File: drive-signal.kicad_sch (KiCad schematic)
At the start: 25 parts, among them J1 Conn_01x03_Pin, J10 Conn_01x04_Pin, J11 Conn_01x04_Pin, J2 Conn_01x03_Pin, J3 Conn_01x03_Pin, J4 Conn_01x03_Pin, J5 Conn_01x03_Pin, J6 Conn_01x03_Pin, J7 Conn_01x02_Pin, J8 Conn_01x04_Pin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

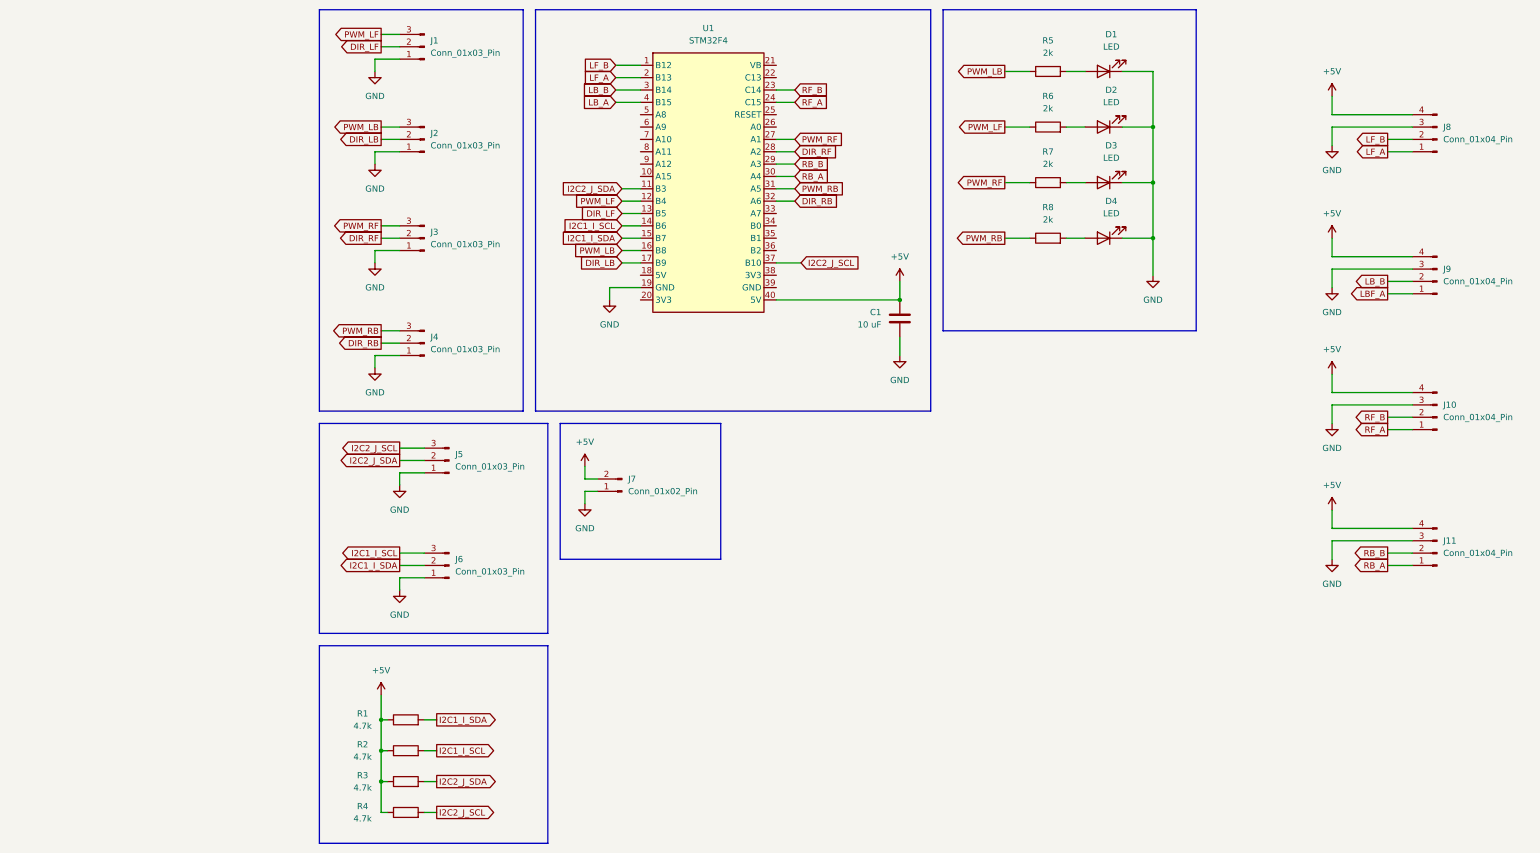
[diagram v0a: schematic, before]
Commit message: fix MD30 pinout
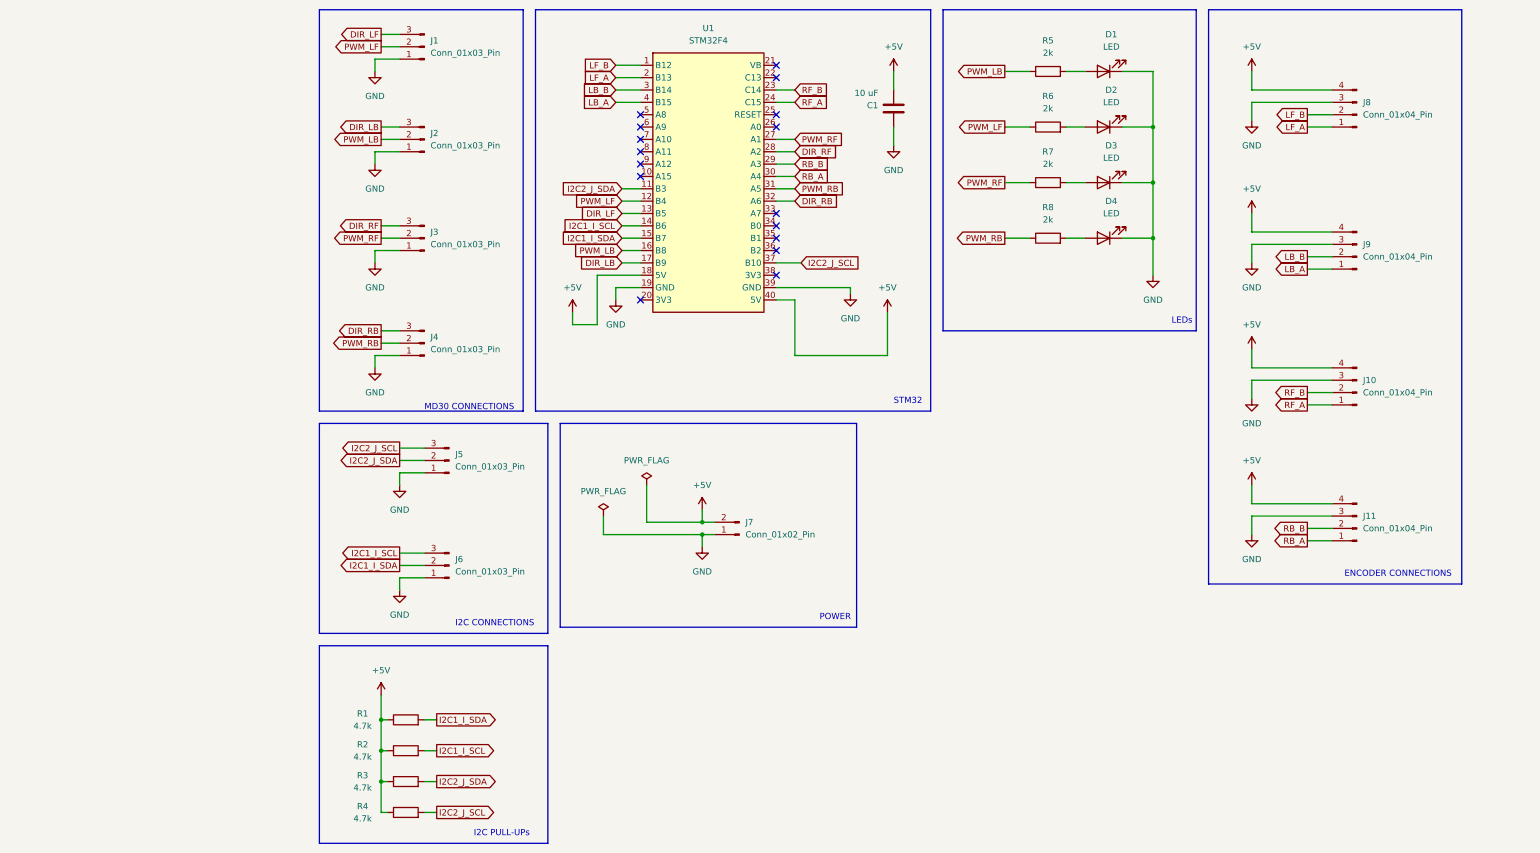
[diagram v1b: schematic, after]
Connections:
- net LBF_A is gone; now on net LB_A: J9.1 (Pin_1)
- net +5V: now also U1.18 (5V)
- net DIR_LB: now also J2.3 (Pin_3); no longer J2.2 (Pin_2)
- net DIR_LF: now also J1.3 (Pin_3); no longer J1.2 (Pin_2)
- net DIR_RB: now also J4.3 (Pin_3); no longer J4.2 (Pin_2)
- net DIR_RF: now also J3.3 (Pin_3); no longer J3.2 (Pin_2)
- net GND: now also U1.39 (GND)
- net PWM_LB: now also J2.2 (Pin_2); no longer J2.3 (Pin_3)
- net PWM_LF: now also J1.2 (Pin_2); no longer J1.3 (Pin_3)
- net PWM_RB: now also J4.2 (Pin_2); no longer J4.3 (Pin_3)
- net PWM_RF: now also J3.2 (Pin_2); no longer J3.3 (Pin_3)
- no-connect marks 0 -> 16
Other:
- note added: "ENCODER CONNECTIONS"
- note added: "I2C CONNECTIONS"
- note added: "I2C PULL-UPs"
- note added: "LEDs"
- note added: "MD30 CONNECTIONS"
- note added: "POWER"
- note added: "STM32"
- company: (none) -> Team RoverX
- title: (none) -> Drive Signal
- moved on the sheet: C1, J10, J11, J7, J8, J9

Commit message: incorporate feedback
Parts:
- J6: value Conn_01x03_Pin -> Conn_01x04_Pin; footprint Connector_JST:JST_PH_B3B-PH-K_1x03_P2.00mm_Vertical -> Connector_JST:JST_PH_B4B-PH-K_1x04_P2.00mm_Vertical; symbol Connector:Conn_01x03_Pin -> Connector:Conn_01x04_Pin
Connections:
- net +5V: now also J6.2 (Pin_2)
- net I2C1_I_SCL: now also J6.4 (Pin_4); no longer J6.3 (Pin_3)
- net I2C1_I_SDA: now also J6.3 (Pin_3); no longer J6.2 (Pin_2)
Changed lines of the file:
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@@
+    (stroke (width 0) (type default))
+  )
+  (wire (pts (xy 17.78 128.27) (xy 35.56 128.27))
     (stroke (width 0) (type default))
   )
@@
     (stroke (width 0) (type default))
   )
+  (wire (pts (xy 17.78 120.65) (xy 17.78 128.27))
+    (stroke (width 0) (type default))
+  )
   (wire (pts (xy 30.48 43.18) (xy 25.4 43.18))
     (stroke (width 0) (type default))
@@
     (stroke (width 0) (type default))
   )
-  (wire (pts (xy 30.48 128.27) (xy 35.56 128.27))
-    (stroke (width 0) (type default))
-  )
   (wire (pts (xy 26.67 160.02) (xy 26.67 166.37))
     (stroke (width 0) (type default))
@@
     (stroke (width 0) (type default))
   )
+  (wire (pts (xy 33.02 123.19) (xy 35.56 123.19))
+    (stroke (width 0) (type default))
+  )
   (wire (pts (xy 74.93 33.02) (xy 80.01 33.02))
     (stroke (width 0) (type default))
   )
+  (wire (pts (xy 33.02 125.73) (xy 35.56 125.73))
+    (stroke (width 0) (type default))
+  )
   (wire (pts (xy 30.48 106.68) (xy 35.56 106.68))
     (stroke (width 0) (type default))
@@
   )
   (wire (pts (xy 26.67 60.96) (xy 30.48 60.96))
-    (stroke (width 0) (type default))
-  )
-  (wire (pts (xy 30.48 125.73) (xy 35.56 125.73))
     (stroke (width 0) (type default))
   )
@@
     )
   )
-  (global_label "I2C1_I_SDA" (shape output) (at 30.48 128.27 180) (fields_autoplaced)
-    (effects (font (size 1.27 1.27)) (justify right))
-    (property "Intersheetrefs" "${INTERSHEET_REFS}" (at 17.0929 128.27 0)
+  (global_label "I2C1_I_SDA" (shape output) (at 33.02 125.73 180) (fields_autoplaced)
+    (effects (font (size 1.27 1.27)) (justify right))
+    (property "Intersheetrefs" "${INTERSHEET_REFS}" (at 19.6329 125.73 0)
       (effects (font (size 1.27 1.27)) (justify right) hide)
     )
@@
     )
   )
-  (global_label "I2C1_I_SCL" (shape output) (at 30.48 125.73 180) (fields_autoplaced)
-    (effects (font (size 1.27 1.27)) (justify right))
-    (property "Intersheetrefs" "${INTERSHEET_REFS}" (at 17.1534 125.73 0)
+  (global_label "I2C1_I_SCL" (shape output) (at 33.02 123.19 180) (fields_autoplaced)
+    (effects (font (size 1.27 1.27)) (justify right))
+    (property "Intersheetrefs" "${INTERSHEET_REFS}" (at 19.6934 123.19 0)
       (effects (font (size 1.27 1.27)) (justify right) hide)
     )
@@
     )
   )
-  (symbol (lib_id "Connector:Conn_01x03_Pin") (at 40.64 128.27 180) (unit 1)
-    (in_bom yes) (on_board yes) (dnp no) (fields_autoplaced)
-    (property "Reference" "J6" (at 41.91 127 0)
-      (effects (font (size 1.27 1.27)) (justify right))
-    )
-    (property "Value" "Conn_01x03_Pin" (at 41.91 129.54 0)
-      (effects (font (size 1.27 1.27)) (justify right))
-    )
-    (property "Footprint" "Connector_JST:JST_PH_B3B-PH-K_1x03_P2.00mm_Vertical" (at 40.64 128.27 0)
+  (symbol (lib_id "Connector:Conn_01x04_Pin") (at 40.64 128.27 180) (unit 1)
+    (in_bom yes) (on_board yes) (dnp no) (fields_autoplaced)
+    (property "Reference" "J6" (at 41.91 125.73 0)
+      (effects (font (size 1.27 1.27)) (justify right))
+    )
+    (property "Value" "Conn_01x04_Pin" (at 41.91 128.27 0)
+      (effects (font (size 1.27 1.27)) (justify right))
+    )
+    (property "Footprint" "Connector_JST:JST_PH_B4B-PH-K_1x04_P2.00mm_Vertical" (at 40.64 128.27 0)
       (effects (font (size 1.27 1.27)) hide)
     )
@@
     (pin "1")
     (pin "3")
+    (pin "4")
     (instances
       (project "drive-signal"
@@
         )
       )
+    )
+  )
+  (symbol (lib_id "power:+5V") (at 17.78 120.65 0) (unit 1)
+    (in_bom yes) (on_board yes) (dnp no) (fields_autoplaced)
+    (property "Reference" "#PWR025" (at 17.78 124.46 0)
+      (effects (font (size 1.27 1.27)) hide)
+    )
+    (property "Value" "+5V" (at 17.78 115.57 0)
+      (effects (font (size 1.27 1.27)))
+    )
+    (property "Footprint" "" (at 17.78 120.65 0)
+      (effects (font (size 1.27 1.27)) hide)
+    )
+    (property "Datasheet" "" (at 17.78 120.65 0)
+      (effects (font (size 1.27 1.27)) hide)
+    )
+    (pin "1")
+    (instances
+      (project "drive-signal"
+        (path "/0fd5a227-32c1-4fb8-b9b0-22b52f16b2f2"
+          (reference "#PWR025") (unit 1)
+        )
+      )

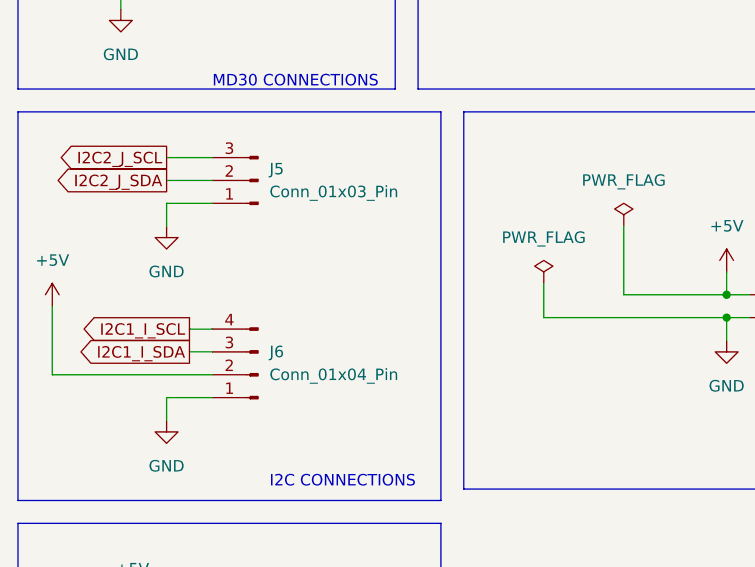
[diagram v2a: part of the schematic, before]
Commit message: make JSTs horizontal
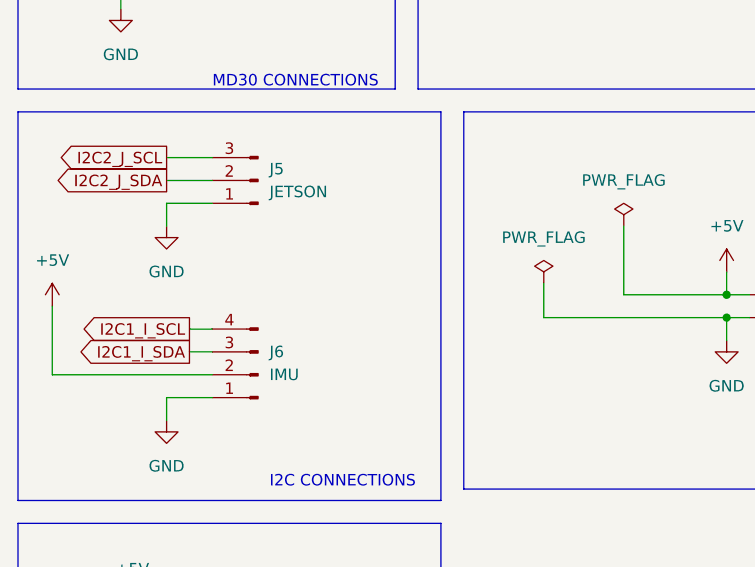
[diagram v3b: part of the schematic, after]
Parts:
- J1, J2, J3, J4: footprint Connector_JST:JST_PH_B3B-PH-K_1x03_P2.00mm_Vertical -> Connector_JST:JST_PH_S3B-PH-K_1x03_P2.00mm_Horizontal
- J10, J11, J8, J9: footprint Connector_JST:JST_PH_B4B-PH-K_1x04_P2.00mm_Vertical -> Connector_JST:JST_PH_S4B-PH-K_1x04_P2.00mm_Horizontal
- J5: value Conn_01x03_Pin -> JETSON
- J6: value Conn_01x04_Pin -> IMU
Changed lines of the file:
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@@
       (effects (font (size 1.27 1.27)) (justify right))
     )
-    (property "Footprint" "Connector_JST:JST_PH_B4B-PH-K_1x04_P2.00mm_Vertical" (at 227.33 35.56 0)
+    (property "Footprint" "Connector_JST:JST_PH_S4B-PH-K_1x04_P2.00mm_Horizontal" (at 227.33 35.56 0)
       (effects (font (size 1.27 1.27)) hide)
     )
@@
       (effects (font (size 1.27 1.27)) (justify right))
     )
-    (property "Footprint" "Connector_JST:JST_PH_B4B-PH-K_1x04_P2.00mm_Vertical" (at 227.33 120.65 0)
+    (property "Footprint" "Connector_JST:JST_PH_S4B-PH-K_1x04_P2.00mm_Horizontal" (at 227.33 120.65 0)
       (effects (font (size 1.27 1.27)) hide)
     )
@@
       (effects (font (size 1.27 1.27)) (justify right))
     )
-    (property "Footprint" "Connector_JST:JST_PH_B4B-PH-K_1x04_P2.00mm_Vertical" (at 227.33 92.71 0)
+    (property "Footprint" "Connector_JST:JST_PH_S4B-PH-K_1x04_P2.00mm_Horizontal" (at 227.33 92.71 0)
       (effects (font (size 1.27 1.27)) hide)
     )
@@
       (effects (font (size 1.27 1.27)) (justify right))
     )
-    (property "Value" "Conn_01x04_Pin" (at 41.91 128.27 0)
+    (property "Value" "IMU" (at 41.91 128.27 0)
       (effects (font (size 1.27 1.27)) (justify right))
     )
@@
       (effects (font (size 1.27 1.27)) (justify right))
     )
-    (property "Footprint" "Connector_JST:JST_PH_B3B-PH-K_1x03_P2.00mm_Vertical" (at 35.56 40.64 0)
+    (property "Footprint" "Connector_JST:JST_PH_S3B-PH-K_1x03_P2.00mm_Horizontal" (at 35.56 40.64 0)
       (effects (font (size 1.27 1.27)) hide)
     )
@@
       (effects (font (size 1.27 1.27)) (justify right))
     )
-    (property "Footprint" "Connector_JST:JST_PH_B4B-PH-K_1x04_P2.00mm_Vertical" (at 227.33 64.77 0)
+    (property "Footprint" "Connector_JST:JST_PH_S4B-PH-K_1x04_P2.00mm_Horizontal" (at 227.33 64.77 0)
       (effects (font (size 1.27 1.27)) hide)
     )
@@
       (effects (font (size 1.27 1.27)) (justify right))
     )
-    (property "Footprint" "Connector_JST:JST_PH_B3B-PH-K_1x03_P2.00mm_Vertical" (at 35.56 60.96 0)
+    (property "Footprint" "Connector_JST:JST_PH_S3B-PH-K_1x03_P2.00mm_Horizontal" (at 35.56 60.96 0)
       (effects (font (size 1.27 1.27)) hide)
     )
@@
       (effects (font (size 1.27 1.27)) (justify right))
     )
-    (property "Footprint" "Connector_JST:JST_PH_B3B-PH-K_1x03_P2.00mm_Vertical" (at 35.56 21.59 0)
+    (property "Footprint" "Connector_JST:JST_PH_S3B-PH-K_1x03_P2.00mm_Horizontal" (at 35.56 21.59 0)
       (effects (font (size 1.27 1.27)) hide)
     )
@@
       (effects (font (size 1.27 1.27)) (justify right))
     )
-    (property "Value" "Conn_01x03_Pin" (at 41.91 107.95 0)
+    (property "Value" "JETSON" (at 41.91 107.95 0)
       (effects (font (size 1.27 1.27)) (justify right))
     )
@@
       (effects (font (size 1.27 1.27)) (justify right))
     )
-    (property "Footprint" "Connector_JST:JST_PH_B3B-PH-K_1x03_P2.00mm_Vertical" (at 35.56 82.55 0)
-      (effects (font (size 1.27 1.27)) hide)
-    )
+    (property "Footprint" "Connector_JST:JST_PH_S3B-PH-K_1x03_P2.00mm_Horizontal" (at 35.56 82.55 0)
+      (effects (font (size 1.27 1.27)) hide)
+    )
